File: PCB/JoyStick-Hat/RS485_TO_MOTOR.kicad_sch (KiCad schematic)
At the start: 16 parts, among them J5 RJHSE-5381, U4 MAX3535ECWI+T

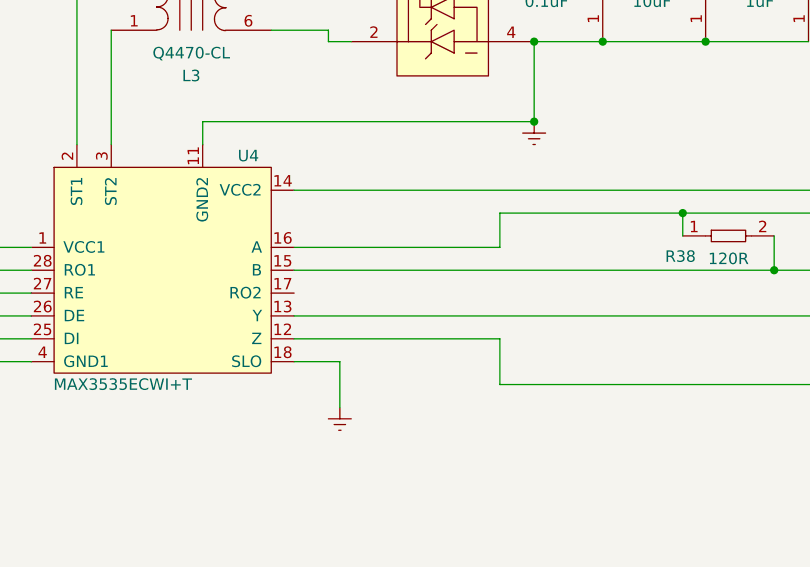
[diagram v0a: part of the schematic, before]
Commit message: Board Tweaks
Copper pour specifications adjusted and repoured. DRC errors are caused by silkscreen , this happened when updating from KiCAD 7 to 8, still investigating it.
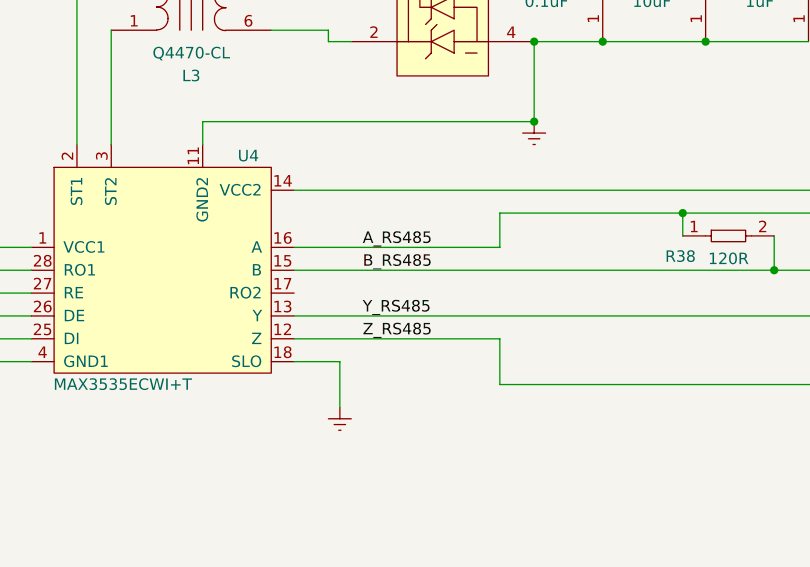
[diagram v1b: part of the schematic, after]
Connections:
- net A_RS485: now reaches J5.1, R38.1, U4.16 (A)
- net B_RS485: now reaches J5.2, R38.2, U4.15 (B)
- net Y_RS485: now reaches J5.7, U4.13 (Y)
- net Z_RS485: now reaches J5.8, U4.12 (Z)
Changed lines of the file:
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@@
+		)
+	)
+	(label "B_RS485"
+		(at 175.26 99.06 0)
+		(fields_autoplaced yes)
+		(effects
+			(font
+				(size 1.27 1.27)
+			)
+			(justify left bottom)
 		)
 	)
@@
 		(fields_autoplaced yes)
 		(effects
+			(font
+				(size 1.27 1.27)
+			)
+			(justify left bottom)
+		)
+	)
+	(label "Z_RS485"
+		(at 175.26 106.68 0)
+		(fields_autoplaced yes)
+		(effects
+			(font
+				(size 1.27 1.27)
+			)
+			(justify left bottom)
+		)
+	)
+	(label "A_RS485"
+		(at 175.26 96.52 0)
+		(fields_autoplaced yes)
+		(effects
+			(font
+				(size 1.27 1.27)
+			)
+			(justify left bottom)
+		)
+	)
+	(label "Y_RS485"
+		(at 175.26 104.14 0)
+		(fields_autoplaced yes)
+		(effects
